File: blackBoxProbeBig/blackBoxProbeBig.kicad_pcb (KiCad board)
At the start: 4 copper layers, 44 x 44 mm, 84 parts, among them J1 USB-ID, J2 JTAG_2X05, J3 JTAG_2X05, J4 Conn_01x04, Q1 Q_NMOS_DUAL, Q2 Q_PMOS_DUAL, U1 MCP1702-MB, U2 USBLC6-2, U3 STM32F103CBT, U4 74X2T45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

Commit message: added pcblibrary submodule
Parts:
- removed R17: 1K, SquantorRcl:R_0603_hand
- removed R19: 10, SquantorRcl:R_0603_hand
- removed R2, R3: R, SquantorRcl:R_0603_hand
- removed R23: 10K, SquantorRcl:R_0603_hand
- N2: value V20180728 -> V20181130
- R36: value 100 -> 22
- moved R18 3.00 mm to (17.5, 187.0)
- moved C10 2.33 mm to (20.5, 187.0)
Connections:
- J1 pad 4: Net-(J1-Pad4) -> GND
- J2 pad 1: Net-(J2-Pad1) -> +3V3
- R20 pad 1: /PROBE_VDD -> /PROBE_E_VDD
- U3 pad 44: Net-(R17-Pad2) -> GND
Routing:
- net Net-(J2-Pad1): track 9.27 -> 0.00 mm
- net +3V3: track 52.2 -> 59.8 mm, vias 18 -> 16
- net Net-(J1-Pad4): track 6.11 -> 0.00 mm
- net Net-(R17-Pad2): track 5.48 -> 0.00 mm
- net GND: track 82.9 -> 87.2 mm
- net /PROBE_E_VDD: track 35.7 -> 38.1 mm
- net /MCU_RST: track 16.1 -> 17.4 mm
- net /PROBE_VDD: track 48.4 -> 47.5 mm

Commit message: schematic simplifications, regulator rework, silk movements
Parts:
- removed C3: 100n, SquantorRcl:C_0603
- U1: footprint SquantorMicrochip:MB-(SOT-89) -> SquantorIC:SOT89-ViaTab-Microchip-MB
- moved C4 7.12 mm to (18.1, 153.8), turned to 0 degrees
- moved C1 3.60 mm to (18.1, 161.5)
- moved U1 1.75 mm to (18.1, 156.1), turned to 180 degrees
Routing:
- net +3V3: track 59.8 -> 70.7 mm
- net GND: track 87.2 -> 81.7 mm, vias 22 -> 21
- net +5V: track 29.9 -> 24.6 mm, vias 3 -> 2
- added copper zone on B.Cu, net +5V
- removed copper zone on F.Cu, net +5V

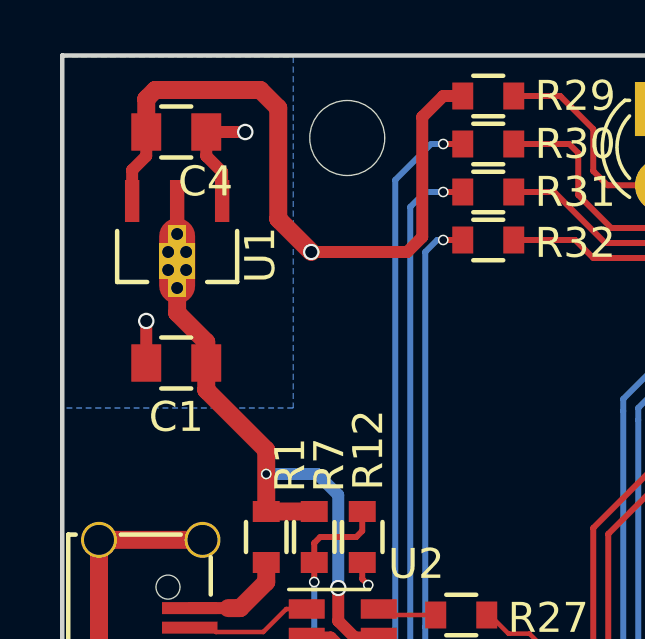
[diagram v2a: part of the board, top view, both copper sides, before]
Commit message: updated component footprints
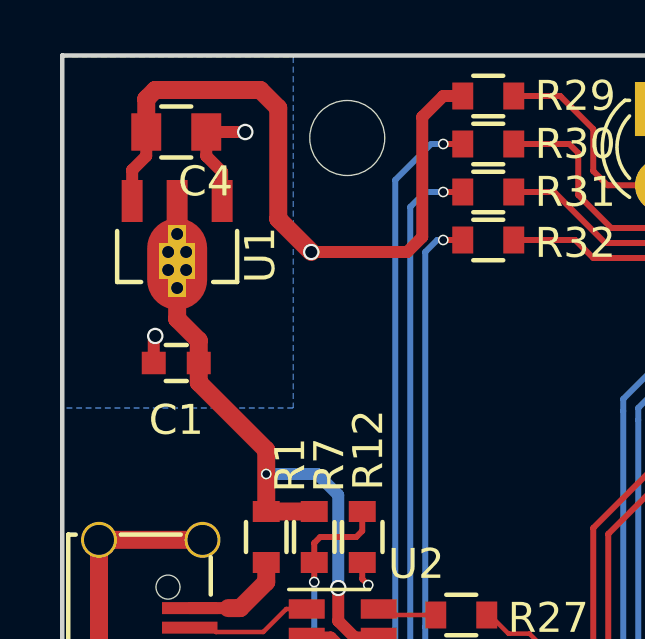
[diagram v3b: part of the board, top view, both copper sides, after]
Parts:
- C1: value 2.2u -> 1u; footprint SquantorRcl:C_0805 -> SquantorRcl:C_0603
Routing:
- net +5V: track 24.6 -> 24.0 mm
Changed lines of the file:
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@@
     (thickness 1.6)
     (drawings 10)
-    (tracks 764)
+    (tracks 765)
     (zones 0)
     (modules 78)
@@
   )
   (setup
-    (last_trace_width 0.4)
+    (last_trace_width 0.6)
     (user_trace_width 0.1524)
     (user_trace_width 0.2)
@@
     (add_net VDDA)
   )
+  (module SquantorIC:SOT89-ViaTab-Microchip-MB (layer F.Cu)
+    (at 18.13 156.1 180)
+    (fp_text reference U1 (at -2.77 -1.8 270) (layer F.SilkS)
+      (effects (font (size 1 1) (thickness 0.15)))
+    )
+    (fp_text value MCP1702-MB (at 0 2 180) (layer F.Fab)
+      (effects (font (size 1 1) (thickness 0.15)))
+    )
+    (fp_line (start 2 -2.7) (end 2 -1) (layer F.SilkS) (width 0.15))
+    (fp_line (start 1.2 -2.7) (end 2 -2.7) (layer F.SilkS) (width 0.15))
+    (fp_line (start -2 -2.7) (end -1.2 -2.7) (layer F.SilkS) (width 0.15))
+    (fp_line (start -2 -1) (end -2 -2.7) (layer F.SilkS) (width 0.15))
+    (pad 1 smd rect (at -1.5 0 180) (size 0.7 1.4) (layers F.Cu F.Paste F.Mask)
+      (net 2 GND))
+    (pad 2 smd rect (at 0 0 180) (size 0.7 1.4) (layers F.Cu F.Paste F.Mask)
+      (net 1 +5V))
+    (pad 3 smd rect (at 1.5 0 180) (size 0.7 1.4) (layers F.Cu F.Paste F.Mask)
+      (net 4 +3V3))
+    (pad TAB smd oval (at 0 -2.1 180) (size 2 3.05) (layers F.Cu F.Paste F.Mask)
+      (net 1 +5V) (zone_connect 2))
+    (pad TAB thru_hole rect (at -0.3 -1.7 180) (size 0.6 0.6) (drill 0.4) (layers *.Cu *.Mask)
+      (net 1 +5V) (zone_connect 2))
+    (pad TAB thru_hole rect (at 0.3 -1.7 180) (size 0.6 0.6) (drill 0.4) (layers *.Cu *.Mask)
+      (net 1 +5V) (zone_connect 2))
+    (pad TAB thru_hole rect (at 0.3 -2.3 180) (size 0.6 0.6) (drill 0.4) (layers *.Cu *.Mask)
+      (net 1 +5V) (zone_connect 2))
+    (pad TAB thru_hole rect (at -0.3 -2.3 180) (size 0.6 0.6) (drill 0.4) (layers *.Cu *.Mask)
+      (net 1 +5V) (zone_connect 2))
+    (pad TAB thru_hole rect (at 0 -2.9 180) (size 0.6 0.6) (drill 0.4) (layers *.Cu *.Mask)
+      (net 1 +5V) (zone_connect 2))
+    (pad TAB thru_hole rect (at 0 -1.1 180) (size 0.6 0.6) (drill 0.4) (layers *.Cu *.Mask)
+      (net 1 +5V) (zone_connect 2))
+  )
   (module SquantorConnectors:Header-0127-2X05-H006 (layer F.Cu)
     (at 17.3 182.2 270)
@@
   )
   (module SquantorRcl:C_0805 (layer F.Cu)
-    (at 18.1 161.5 180)
-    (descr "Capacitor SMD 0805, reflow soldering, AVX (see smccp.pdf)")
-    (tags "capacitor 0805")
-    (attr smd)
-    (fp_text reference C1 (at 0 -1.8 180) (layer F.SilkS)
-      (effects (font (size 1 1) (thickness 0.15)))
-    )
-    (fp_text value 2.2u (at -6.35 0.1 180) (layer F.Fab)
-      (effects (font (size 1 1) (thickness 0.15)))
-    )
-    (fp_line (start -1 0.625) (end -1 -0.625) (layer F.Fab) (width 0.15))
-    (fp_line (start 1 0.625) (end -1 0.625) (layer F.Fab) (width 0.15))
-    (fp_line (start 1 -0.625) (end 1 0.625) (layer F.Fab) (width 0.15))
-    (fp_line (start -1 -0.625) (end 1 -0.625) (layer F.Fab) (width 0.15))
-    (fp_line (start -1.8 -1) (end 1.8 -1) (layer F.CrtYd) (width 0.05))
-    (fp_line (start -1.8 1) (end 1.8 1) (layer F.CrtYd) (width 0.05))
-    (fp_line (start -1.8 -1) (end -1.8 1) (layer F.CrtYd) (width 0.05))
-    (fp_line (start 1.8 -1) (end 1.8 1) (layer F.CrtYd) (width 0.05))
-    (fp_line (start 0.5 -0.85) (end -0.5 -0.85) (layer F.SilkS) (width 0.15))
-    (fp_line (start -0.5 0.85) (end 0.5 0.85) (layer F.SilkS) (width 0.15))
-    (pad 1 smd rect (at -1 0 180) (size 1 1.25) (layers F.Cu F.Paste F.Mask)
-      (net 1 +5V))
-    (pad 2 smd rect (at 1 0 180) (size 1 1.25) (layers F.Cu F.Paste F.Mask)
-      (net 2 GND))
-    (model Capacitors_SMD.3dshapes/C_0805.wrl
-      (at (xyz 0 0 0))
-      (scale (xyz 1 1 1))
-      (rotate (xyz 0 0 0))
-    )
-  )
-  (module SquantorRcl:C_0805 (layer F.Cu)
     (at 17.21 176.69)
     (descr "Capacitor SMD 0805, reflow soldering, AVX (see smccp.pdf)")
@@
       (net 63 /PROBE_E_VDD))
   )
-  (module SquantorIC:SOT89-ViaTab-Microchip-MB (layer F.Cu)
-    (at 18.13 156.1 180)
-    (fp_text reference U1 (at -2.77 -1.8 270) (layer F.SilkS)
+  (module SquantorRcl:C_0603 (layer F.Cu)
+    (at 18.1 161.5 180)
+    (descr "Capacitor SMD 0603, reflow soldering, AVX (see smccp.pdf)")
+    (tags "capacitor 0603")
+    (attr smd)
+    (fp_text reference C1 (at 0 -1.9 180) (layer F.SilkS)
       (effects (font (size 1 1) (thickness 0.15)))
     )
-    (fp_text value MCP1702-MB (at 0 2 180) (layer F.Fab)
+    (fp_text value 1u (at 0 1.9 180) (layer F.Fab)
       (effects (font (size 1 1) (thickness 0.15)))
     )
-    (fp_line (start 2 -2.7) (end 2 -1) (layer F.SilkS) (width 0.15))
-    (fp_line (start 1 -2.7) (end 2 -2.7) (layer F.SilkS) (width 0.15))
-    (fp_line (start -2 -2.7) (end -1 -2.7) (layer F.SilkS) (width 0.15))
-    (fp_line (start -2 -1) (end -2 -2.7) (layer F.SilkS) (width 0.15))
-    (pad 1 smd rect (at -1.5 0 180) (size 0.48 1.4) (layers F.Cu F.Paste F.Mask)
-      (net 2 GND))
-    (pad 2 smd rect (at 0 0 180) (size 0.48 1.4) (layers F.Cu F.Paste F.Mask)
+    (fp_line (start -0.8 0.4) (end -0.8 -0.4) (layer F.Fab) (width 0.15))
+    (fp_line (start 0.8 0.4) (end -0.8 0.4) (layer F.Fab) (width 0.15))
+    (fp_line (start 0.8 -0.4) (end 0.8 0.4) (layer F.Fab) (width 0.15))
+    (fp_line (start -0.8 -0.4) (end 0.8 -0.4) (layer F.Fab) (width 0.15))
+    (fp_line (start -1.45 -0.75) (end 1.45 -0.75) (layer F.CrtYd) (width 0.05))
+    (fp_line (start -1.45 0.75) (end 1.45 0.75) (layer F.CrtYd) (width 0.05))
+    (fp_line (start -1.45 -0.75) (end -1.45 0.75) (layer F.CrtYd) (width 0.05))
+    (fp_line (start 1.45 -0.75) (end 1.45 0.75) (layer F.CrtYd) (width 0.05))
+    (fp_line (start -0.35 -0.6) (end 0.35 -0.6) (layer F.SilkS) (width 0.15))
+    (fp_line (start 0.35 0.6) (end -0.35 0.6) (layer F.SilkS) (width 0.15))
+    (pad 1 smd rect (at -0.75 0 180) (size 0.8 0.75) (layers F.Cu F.Paste F.Mask)
       (net 1 +5V))
-    (pad 3 smd rect (at 1.5 0 180) (size 0.48 1.4) (layers F.Cu F.Paste F.Mask)
-      (net 4 +3V3))
-    (pad TAB smd oval (at 0 -2 180) (size 1.2 2.85) (layers F.Cu F.Paste F.Mask)
-      (net 1 +5V) (zone_connect 2))
-    (pad TAB thru_hole rect (at -0.3 -1.7 180) (size 0.6 0.6) (drill 0.4) (layers *.Cu *.Mask)
-      (net 1 +5V) (zone_connect 2))
-    (pad TAB thru_hole rect (at 0.3 -1.7 180) (size 0.6 0.6) (drill 0.4) (layers *.Cu *.Mask)
-      (net 1 +5V) (zone_connect 2))
-    (pad TAB thru_hole rect (at 0.3 -2.3 180) (size 0.6 0.6) (drill 0.4) (layers *.Cu *.Mask)
-      (net 1 +5V) (zone_connect 2))
-    (pad TAB thru_hole rect (at -0.3 -2.3 180) (size 0.6 0.6) (drill 0.4) (layers *.Cu *.Mask)
-      (net 1 +5V) (zone_connect 2))
-    (pad TAB thru_hole rect (at 0 -2.9 180) (size 0.6 0.6) (drill 0.4) (layers *.Cu *.Mask)
-      (net 1 +5V) (zone_connect 2))
-    (pad TAB thru_hole rect (at 0 -1.1 180) (size 0.6 0.6) (drill 0.4) (layers *.Cu *.Mask)
-      (net 1 +5V) (zone_connect 2))
+    (pad 2 smd rect (at 0.75 0 180) (size 0.8 0.75) (layers F.Cu F.Paste F.Mask)
+      (net 2 GND))
+    (model Capacitors_SMD.3dshapes/C_0603.wrl
+      (at (xyz 0 0 0))
+      (scale (xyz 1 1 1))
+      (rotate (xyz 0 0 0))
+    )
   )
   (gr_arc (start 17.55 192) (end 17.55 189) (angle 90) (layer Edge.Cuts) (width 0.15))
@@
   (segment (start 18.13 157.9) (end 18.13 158.8) (width 0.4) (layer F.Cu) (net 1))
   (segment (start 18.13 155.9) (end 18.13 158.8) (width 0.4) (layer F.Cu) (net 1))
-  (segment (start 21.1 166.45) (end 21.1 164.4) (width 0.6) (layer F.Cu) (net 1))
-  (segment (start 19.1 162.4) (end 19.1 160.9) (width 0.6) (layer F.Cu) (net 1))
-  (segment (start 21.1 164.4) (end 19.1 162.4) (width 0.6) (layer F.Cu) (net 1))
   (segment (start 18.13 157.9) (end 18.13 157) (width 0.6) (layer F.Cu) (net 1))
   (segment (start 22.8 165.2) (end 21.1 165.2) (width 0.4) (layer B.Cu) (net 1))
   (via (at 21.1 165.2) (size 0.3556) (drill 0.254) (layers F.Cu B.Cu) (net 1))
-  (segment (start 19.1 161.5) (end 19.1 160.8) (width 0.6) (layer F.Cu) (net 1))
-  (segment (start 18.13 159.83) (end 18.13 159) (width 0.6) (layer F.Cu) (net 1))
-  (segment (start 19.1 160.8) (end 18.13 159.83) (width 0.6) (layer F.Cu) (net 1))
+  (segment (start 18.85 160.75) (end 18.85 161.5) (width 0.6) (layer F.Cu) (net 1))
+  (segment (start 18.13 159) (end 18.13 160.03) (width 0.6) (layer F.Cu) (net 1))
+  (segment (start 18.13 160.03) (end 18.85 160.75) (width 0.6) (layer F.Cu) (net 1))
+  (segment (start 18.85 162.15) (end 18.85 161.5) (width 0.6) (layer F.Cu) (net 1))
+  (segment (start 21.1 166.45) (end 21.1 164.4) (width 0.6) (layer F.Cu) (net 1))
+  (segment (start 21.1 164.4) (end 18.85 162.15) (width 0.6) (layer F.Cu) (net 1))
   (segment (start 37.5 180.45) (end 35.725 180.45) (width 0.2) (layer F.Cu) (net 2))
   (via (at 38.25 180.45) (size 0.3556) (drill 0.254) (layers F.Cu B.Cu) (net 2))
@@
   (segment (start 19.1 153.8) (end 20.4 153.8) (width 0.4) (layer F.Cu) (net 2))
   (via (at 20.4 153.8) (size 0.55) (drill 0.4) (layers F.Cu B.Cu) (net 2))
-  (segment (start 17.1 160.1) (end 17.1 161.5) (width 0.4) (layer F.Cu) (net 2))
-  (via (at 17.1 160.1) (size 0.55) (drill 0.4) (layers F.Cu B.Cu) (net 2))
+  (via (at 17.4 160.6) (size 0.55) (drill 0.4) (layers F.Cu B.Cu) (net 2))
   (segment (start 19.63 155.13) (end 19.63 156.1) (width 0.4) (layer F.Cu) (net 2))
+  (segment (start 17.35 160.65) (end 17.4 160.6) (width 0.4) (layer F.Cu) (net 2))
+  (segment (start 17.35 161.5) (end 17.35 160.65) (width 0.4) (layer F.Cu) (net 2))
   (segment (start 15.525 167.395) (end 18.975 167.395) (width 0.6) (layer F.Cu) (net 3))
   (segment (start 15.525 174.545) (end 15.525 167.395) (width 0.6) (layer F.Cu) (net 3))
